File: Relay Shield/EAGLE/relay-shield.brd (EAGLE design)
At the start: 81.3 x 83.8 mm, 42 parts, among them IC1 MC33269T-5.0, J1 POWER_JACKSLT, T1 2N3904, T2 2N3904, T3 2N3904, T4 2N3904, U1 RELAYSONGLE, U2 RELAYSONGLE, U3 RELAYSONGLE, U4 RELAYSONGLE

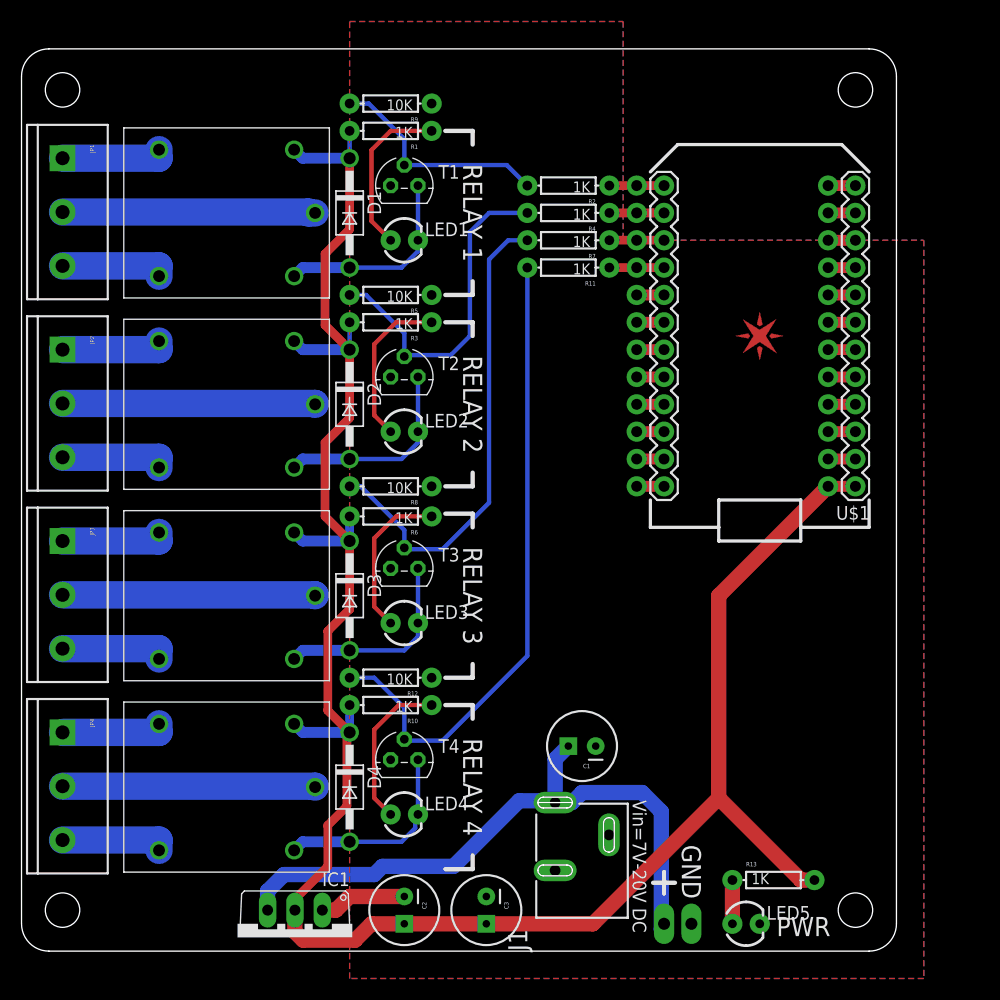
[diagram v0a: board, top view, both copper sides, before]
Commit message: updated shield BOMs and boards
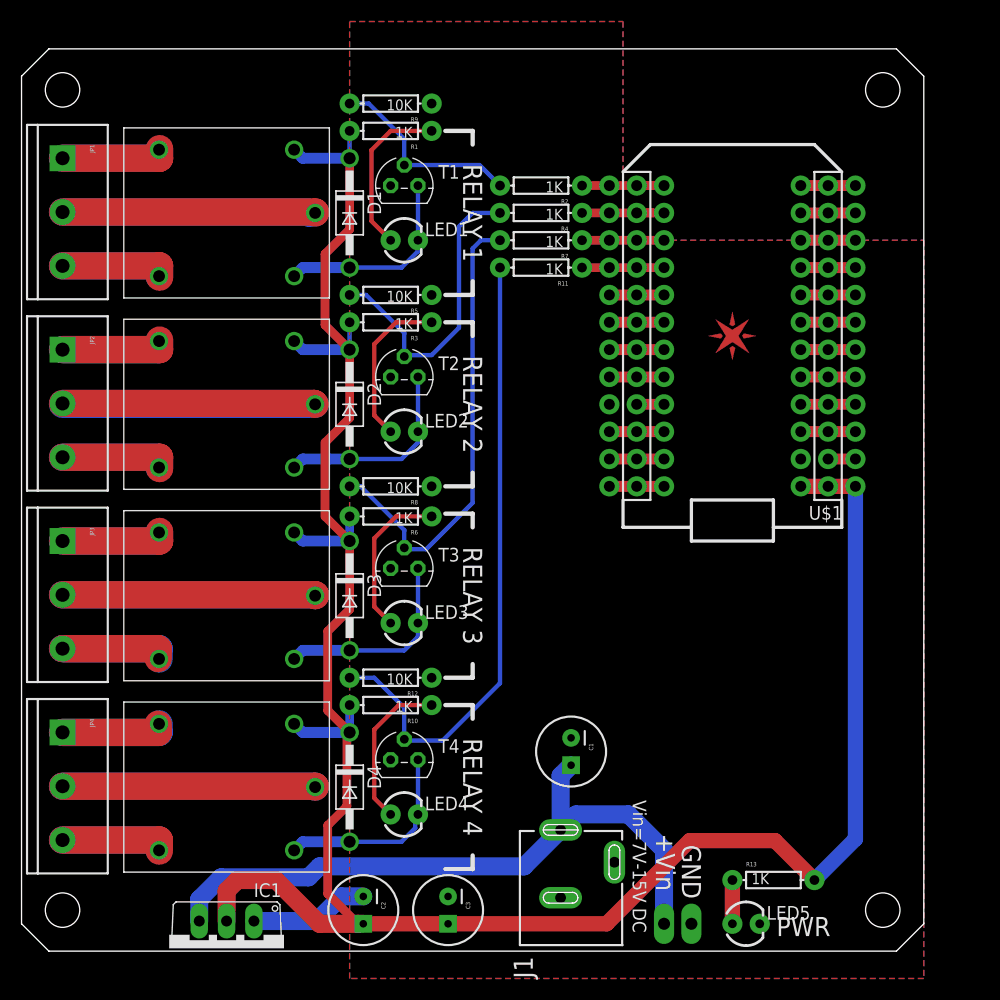
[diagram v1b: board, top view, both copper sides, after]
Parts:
- added LOGO1: OSHW-LOGOM, Spark:OSHW-LOGO-M
- J1: device SparkFun-Connectors:POWER_JACK_SLOT -> Spark:POWER_JACK_SLOT
- LED5: value GREEN -> BLUE
- moved IC1 6.43 mm to (19.1, 0.25)
- moved C2 3.81 mm to (31.8, 3.81)
- moved C3 3.56 mm to (39.6, 3.81)
- moved J1 2.59 mm to (47.5, -2.54)
- moved R11 2.54 mm to (48.3, 63.5)
- moved R2 2.54 mm to (48.3, 71.1)
- moved R4 2.54 mm to (48.3, 68.6)
- moved R7 2.54 mm to (48.3, 66.0)
- moved E$1 2.54 mm to (66.0, 57.1)
- moved U$1 2.54 mm to (66.0, 57.1)
- moved C1 1.14 mm to (51.1, 18.5), turned to 270 degrees
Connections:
- net +5V: now also U$1.#1
- net GND: now also U$1.#2, U$1.#21
- net N$13: now also U$1.#17
- net N$15: now also U$1.#18
- net N$17: now also U$1.#19
- net N$18: now also U$1.#20
- net N$19: now also U$1.#22
- net N$20: now also U$1.#23
- net N$21: now also U$1.#24
- net N$22: now also U$1.#12
- net N$23: now also U$1.#11
- net N$24: now also U$1.#10
- net N$25: now also U$1.#9
- net N$26: now also U$1.#8
- net N$27: now also U$1.#7
- net N$28: now also U$1.#6
- net N$29: now also U$1.#5
- net N$30: now also U$1.#4
- net N$31: now also U$1.#3
- net RELAY1: now also U$1.#13
- net RELAY2: now also U$1.#14
- net RELAY3: now also U$1.#15
- net RELAY4: now also U$1.#16
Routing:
- net MAIN3: track 23.5 -> 47.1 mm
- net MAIN1: track 23.5 -> 47.1 mm
- net MAIN4: track 23.5 -> 47.1 mm
- net MAIN2: track 23.5 -> 47.0 mm
- net +5V: track 204.2 -> 218.4 mm
- net NC2: track 9.92 -> 20.0 mm
- net NC1: track 9.92 -> 20.0 mm
- net NC4: track 9.92 -> 19.9 mm
- net NO1: track 9.76 -> 19.7 mm
- net NO3: track 9.76 -> 19.7 mm
- net NO2: track 9.76 -> 19.7 mm
- net NC3: track 9.92 -> 19.7 mm
- net NO4: track 9.76 -> 19.4 mm
- net RELAY1: track 5.08 -> 9.65 mm
- net RELAY2: track 5.08 -> 9.14 mm
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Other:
- board size 81.3 x 83.8 mm -> 83.8 x 83.8 mm
- board text added: "+Vin"
- board text added: "Relay Shield v2.0 sparkdevices.com"
- board text added: "Vin=7V-15V DC"
- board text removed: "Spark Devices Relay Shield"
- board text removed: "Vin=7V-20V DC"

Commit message: Major hoverhaul to the Relay Shield
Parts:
- removed C1, C2, C3: (no value), SparkFun-Passives:CPOL-RADIAL-100UF-25V
- removed D3, D4: 1N4004, diode:DO41-10
- removed IC1: MC33269T-5.0, linear:TO220V
- removed T1, T2, T3, T4: 2N3904, transistor:TO92
- added C4: 10nF, SparkFun-Capacitors:0603-CAP
- added C5: 47uF, 25V, SparkFun-Capacitors:PANASONIC_D
- added C6: 100uF, 10V, SparkFun-Capacitors:PANASONIC_D
- added D5, D6, D7, D8: (no value), diode:SOD123
- added L1: SDR1005-470KL, Spark:INDUCTOR-SDR1005-470KL
- added Q1, Q2, Q3, Q4: MPSA42, SparkFun-DiscreteSemi:SOT23
- added U$2: LM2672, Spark:SO08
- D1, D2: value 1N4004 -> B230; device diode:DO41-10 -> adafruit:SMADIODE
- LED1, LED2, LED3, LED4, LED5: device SparkFun-LED:LED3MM -> SparkFun-LED:LED-0603
- R1, R10, R11, R12, R13, R2, R3, R4, R5, R6, R7, R8, R9: device SparkFun-Passives:AXIAL-0.3 -> SparkFun-Passives:0603-RES
- U1, U2, U3, U4: value RELAYSONGLE -> RELAYPANASONIC-JS; device Spark:SRD-5VDC-SL-C -> Spark:JS1-5V-F
- moved D1 77.1 mm to (73.4, 4.57), turned to 180 degrees
- moved D2 53.0 mm to (65.0, 10.7), turned to 180 degrees
- moved R11 46.8 mm to (42.4, 17.0)
- moved R7 31.8 mm to (42.4, 34.8)
- moved R4 17.1 mm to (42.2, 52.6)
- moved JP5 14.8 mm to (47.5, 4.32)
- moved R8 14.0 mm to (42.4, 31.8), turned to 0 degrees
- moved R12 14.0 mm to (42.4, 14.0), turned to 0 degrees
- moved R5 13.9 mm to (42.2, 49.5), turned to 0 degrees
- moved R9 13.9 mm to (42.2, 67.3), turned to 0 degrees
- moved LED5 13.0 mm to (80.3, 1.27), turned to 270 degrees
- moved LED3 9.01 mm to (42.4, 36.3), turned to 270 degrees
- moved LED4 9.01 mm to (42.4, 18.5), turned to 270 degrees
- moved R13 8.89 mm to (77.0, 1.27), turned to 180 degrees
- moved LED1 8.82 mm to (42.2, 71.9), turned to 270 degrees
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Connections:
- new net N$32: D2.A, J1.PWR, JP5.2
- new net N$33: C4.1, U$2.1
- new net N$34: C4.2, D1.C, L1.P$1, U$2.8
- net +5V: now also C6.+, D5.C, D6.C, D7.C, D8.C, L1.P$2, R1.2, R10.2, R13.2, R3.2, R6.2, U$2.4; no longer C2.1, C3.1, D1.C, D2.C, D3.C, D4.C, IC1.2, R1.P$2, R10.P$2, R13.P$2, R3.P$2, R6.P$2
- net GND: now also C5.-, C6.-, D1.A, LED5.C, Q1.2, Q2.2, Q3.2, Q4.2, R12.1, R5.1, R8.1, R9.1, U$2.6; no longer C1.2, C2.2, C3.2, IC1.1, LED5.K, R12.P$1, R5.P$1, R8.P$1, R9.P$1, T1.3, T2.3, T3.3, T4.3
- net N$1: now also D5.A, LED1.C, Q1.3; no longer D1.A, LED1.K, T1.1
- net N$10: now also Q4.1, R11.2, R12.2; no longer R11.P$2, R12.P$2, T4.2
- net N$11: now also D8.A, LED4.C, Q4.3; no longer D4.A, LED4.K, T4.1
- net N$12: now also R10.1; no longer R10.P$1
- net N$14: now also C5.+, D2.C, U$2.7; no longer C1.1, IC1.3, J1.PWR, JP5.2
- net N$16: now also R13.1; no longer R13.P$1
- net N$2: now also Q2.1, R4.2, R5.2; no longer R4.P$2, R5.P$2, T2.2
- net N$3: now also Q1.1, R2.2, R9.2; no longer R2.P$2, R9.P$2, T1.2
- net N$4: now also R1.1; no longer R1.P$1
- net N$5: now also D6.A, LED2.C, Q2.3; no longer D2.A, LED2.K, T2.1
- net N$6: now also R3.1; no longer R3.P$1
- net N$7: now also Q3.1, R7.2, R8.2; no longer R7.P$2, R8.P$2, T3.2
- net N$8: now also D7.A, LED3.C, Q3.3; no longer D3.A, LED3.K, T3.1
- net N$9: now also R6.1; no longer R6.P$1
- net RELAY1: now also R2.1; no longer R2.P$1
- net RELAY2: now also R4.1; no longer R4.P$1
- net RELAY3: now also R7.1; no longer R7.P$1
- net RELAY4: now also R11.1; no longer R11.P$1
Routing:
- net RELAY4: track 7.62 -> 62.0 mm
- net N$10: track 58.9 -> 6.33 mm
- net N$14: track 63.1 -> 20.6 mm
- net RELAY3: track 7.62 -> 45.6 mm
- net N$7: track 43.1 -> 6.48 mm
- net N$32: track 0.00 -> 24.8 mm
- net RELAY2: track 9.14 -> 32.6 mm
- net N$2: track 28.6 -> 6.47 mm
- net GND: track 16.2 -> 0.00 mm, vias 0 -> 27
- net +5V: track 218.4 -> 234.5 mm, vias 0 -> 8
- net N$34: track 0.00 -> 12.7 mm
- net N$4: track 15.4 -> 2.87 mm
- net RELAY1: track 9.65 -> 22.1 mm
- net N$3: track 18.5 -> 6.45 mm
- net N$6: track 14.9 -> 2.87 mm
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- added copper zone on layer 1, net +5V
- added copper zone on layer 1, net N$14
- added copper zone on layer 1, net N$34
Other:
- board size 83.8 x 83.8 mm -> 88.9 x 83.8 mm
- board text added: "+"
- board text added: "-"
- board text added: "7V-15V DC"
- board text removed: "+Vin"
- board text removed: "GND"
- board text removed: "Vin=7V-15V DC"
